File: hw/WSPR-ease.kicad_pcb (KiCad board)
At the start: 4 copper layers, 99 x 64 mm, 134 parts, among them J101 SMA, J102 SMA, J103 pwr+data, Q101 MMBF170, Q301 MMBF170, Q302 MMBF170, Q303 MMBF170, Q304 MMBF170, Q305 MMBF170, Q306 MMBF170, Q307 MMBF170, Q308 MMBF170, Q309 MMBF170, Q310 MMBF170, Q311 MMBF170, Q312 MMBF170, T301 BN-43-202_DualPri_CTSec, U101 GNSS module, U102 ESP32-S3-WROOM-1-N8R8, U103 SRV05-4, U104 TPS22918DBVR, U105 TPS74612PQWDRBRQ1, U106 LMR51430YDDCR, U201 AS183-92LF, U202 AS183-92LF, U203 AS183-92LF, U204 AS183-92LF, U301 ICE40UP5K-SG48ITR, U302 CD74ACT541SM96, Y301 40MHz

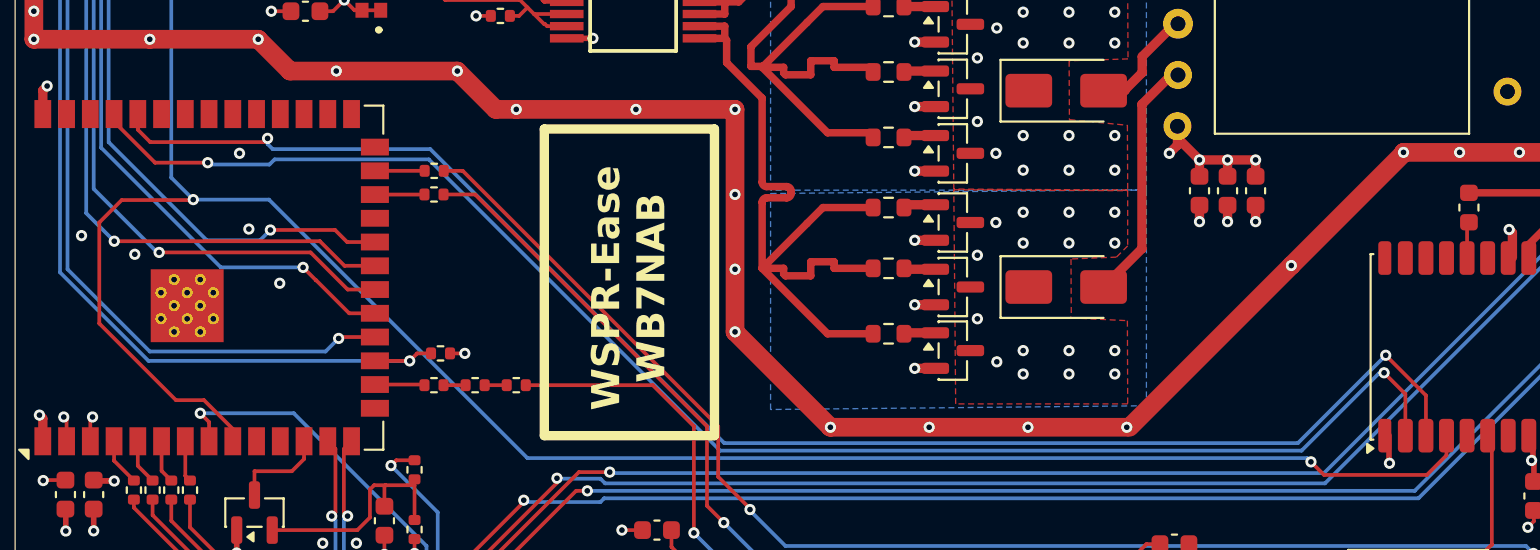
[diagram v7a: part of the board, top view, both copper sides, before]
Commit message: Implement real GNSS hardware integration with reset pulse and UART0 migration
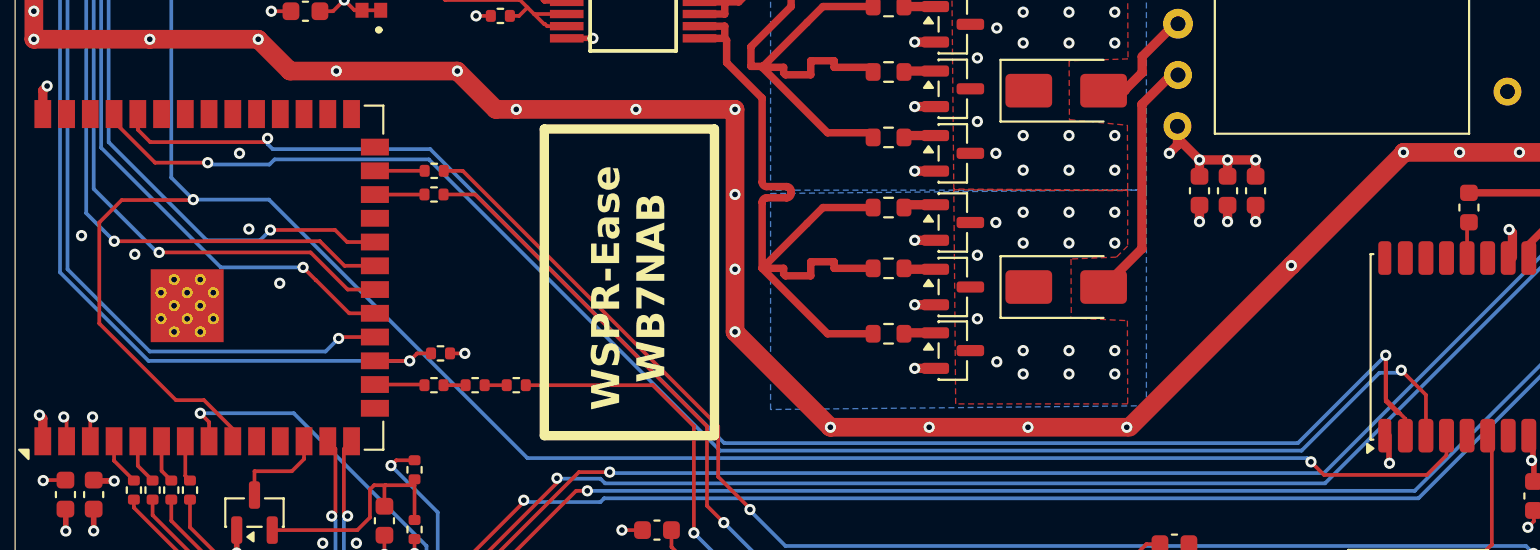
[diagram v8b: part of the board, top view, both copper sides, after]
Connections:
- U101 pad 2: /gnssRx -> /gnssTx
- U101 pad 3: /gnssTx -> /gnssRx
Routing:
- net /gnssTx: track 82.0 -> 85.0 mm
- net /gnssRx: track 81.0 -> 82.6 mm
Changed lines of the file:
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@@
 			(layers "F.Cu" "F.Mask" "F.Paste")
 			(roundrect_rratio 0.25)
-			(net 8 "/gnssRx")
+			(net 9 "/gnssTx")
 			(pinfunction "TXD")
 			(pintype "output")
@@
 			(layers "F.Cu" "F.Mask" "F.Paste")
 			(roundrect_rratio 0.25)
-			(net 9 "/gnssTx")
+			(net 8 "/gnssRx")
 			(pinfunction "RXD")
 			(pintype "input")
@@
 	)
 	(segment
-		(start 57.0829 102.5)
-		(end 54.89 100.3071)
+		(start 123.73 113.6)
+		(end 125.05 114.92)
 		(width 0.2)
 		(layer "F.Cu")
@@
 	)
 	(segment
-		(start 123.95 117.1)
-		(end 123.95 114.875)
+		(start 125.05 114.92)
+		(end 125.05 117.1)
 		(width 0.2)
 		(layer "F.Cu")
@@
 	)
 	(segment
-		(start 59.9 102.5)
+		(start 54.89 100.3071)
 		(end 57.0829 102.5)
 		(width 0.2)
@@
 	)
 	(segment
-		(start 123.95 114.875)
-		(end 122.811765 113.736765)
+		(start 54.89 99.9)
+		(end 54.89 100.3071)
+		(width 0.2)
+		(layer "F.Cu")
+		(net 8)
+	)
+	(segment
+		(start 57.0829 102.5)
+		(end 59.9 102.5)
 		(width 0.2)
 		(layer "F.Cu")
@@
 	)
 	(via
-		(at 122.811765 113.736765)
+		(at 123.73 113.6)
 		(size 0.6)
 		(drill 0.3)
@@
 	)
 	(segment
-		(start 87.3 117.9)
-		(end 71.725 102.325)
+		(start 123.73 113.6)
+		(end 123.593235 113.736765)
 		(width 0.2)
 		(layer "B.Cu")
@@
 	)
 	(segment
-		(start 71.725 102.325)
-		(end 63.475 102.325)
+		(start 118.4 117.9)
+		(end 87.3 117.9)
 		(width 0.2)
 		(layer "B.Cu")
@@
 	)
 	(segment
-		(start 122.811765 113.736765)
-		(end 122.563235 113.736765)
+		(start 63.475 102.325)
+		(end 63.2 102.6)
 		(width 0.2)
 		(layer "B.Cu")
@@
 	)
 	(segment
-		(start 63.475 102.325)
-		(end 63.2 102.6)
+		(start 87.3 117.9)
+		(end 71.725 102.325)
 		(width 0.2)
 		(layer "B.Cu")
@@
 	)
 	(segment
-		(start 60 102.6)
-		(end 59.9 102.5)
+		(start 71.725 102.325)
+		(end 63.475 102.325)
 		(width 0.2)
 		(layer "B.Cu")
@@
 	)
 	(segment
-		(start 118.4 117.9)
-		(end 87.3 117.9)
+		(start 123.593235 113.736765)
+		(end 122.563235 113.736765)
 		(width 0.2)
 		(layer "B.Cu")
@@
 	)
 	(segment
+		(start 60 102.6)
+		(end 59.9 102.5)
+		(width 0.2)
+		(layer "B.Cu")
+		(net 8)
+	)
+	(segment
+		(start 122.9 112.8)
+		(end 122.9 115.15)
+		(width 0.2)
+		(layer "F.Cu")
+		(net 9)
+	)
+	(segment
 		(start 56.825 101.4)
 		(end 56.16 100.735)
@@
 	)
 	(segment
+		(start 122.9 115.262648)
+		(end 123.537352 115.9)
+		(width 0.2)
+		(layer "F.Cu")
+		(net 9)
+	)
+	(segment
+		(start 123.537352 115.9)
+		(end 123.66 115.9)
+		(width 0.2)
+		(layer "F.Cu")
+		(net 9)
+	)
+	(segment
 		(start 56.16 100.735)
 		(end 56.16 99.9)
@@
 	)
 	(segment
-		(start 63.1 101.2)
-		(end 62.9 101.4)
+		(start 122.9 112.8)
+		(end 122.9 115.262648)
 		(width 0.2)
 		(layer "F.Cu")
@@
 	)
 	(segment
-		(start 62.9 101.4)
-		(end 56.825 101.4)
+		(start 123.95 116.2)
+		(end 123.95 117.1)
 		(width 0.2)
 		(layer "F.Cu")
@@
 	)
 	(segment
-		(start 125.05 117.1)
-		(end 125.05 114.95)
+		(start 63.1 101.2)
+		(end 62.9 101.4)
+		(width 0.2)
+		(layer "F.Cu")
+		(net 9)
+	)
+	(segment
+		(start 62.9 101.4)
+		(end 56.825 101.4)
 		(width 0.2)
 		(layer "F.Cu")
@@
 	)
 	(segment
-		(start 125.05 114.95)
-		(end 122.9 112.8)
+		(start 122.9 115.15)
+		(end 123.95 116.2)
 		(width 0.2)
 		(layer "F.Cu")
